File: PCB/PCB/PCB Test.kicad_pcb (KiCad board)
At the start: 2 copper layers, 69 x 30 mm, 53 parts, among them J1 USB_C_Receptacle_USB2.0, J2 Conn_01x06, J3 BATT, Q1 DMN2056U, Q2 Si2329DS, Q3 DMN2056U, Q4 DMG9926UDM, SW1 SW_Push, SW2 SW_Push, U1 24FC64F, U2 STM32L052K6Tx, U3 TUSB320, U4 MIC5366-3.3YC5, U5 BQ297xy, U6 BQ24072RGT

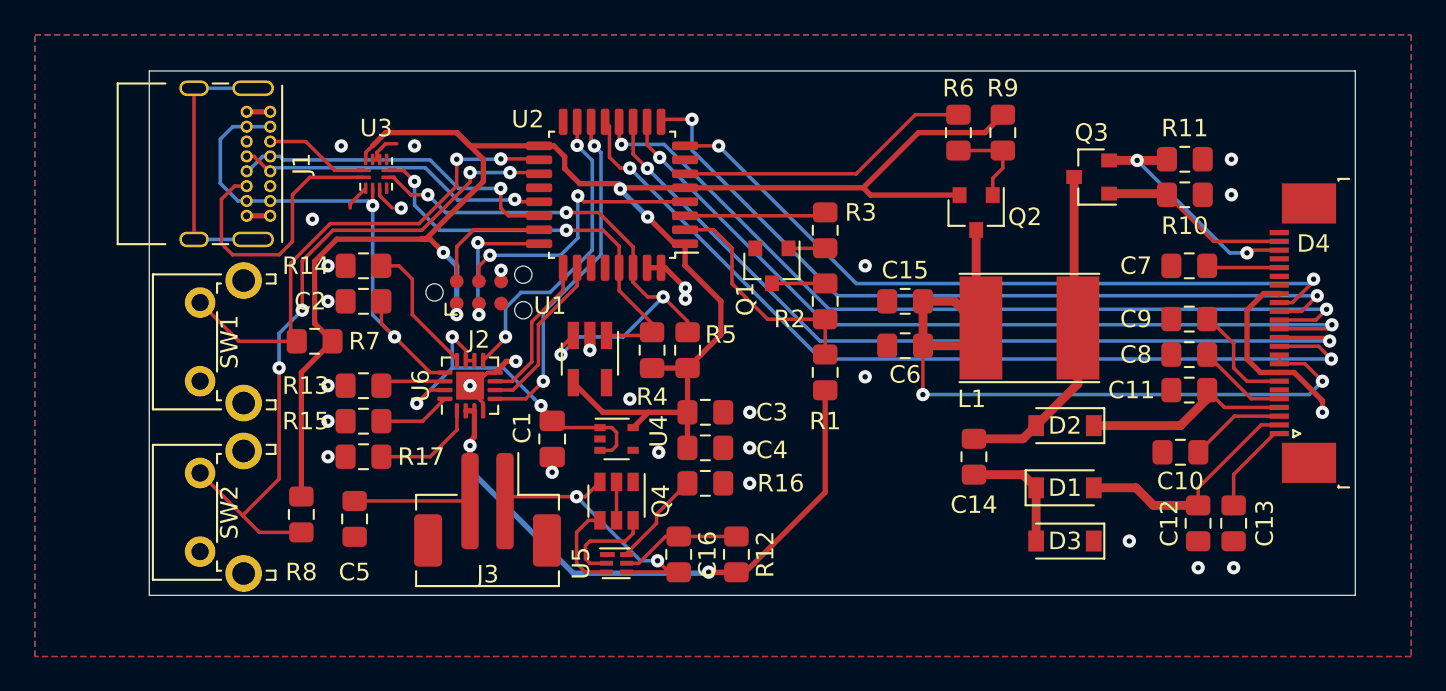
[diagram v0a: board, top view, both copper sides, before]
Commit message: Updated schematic to Rev C
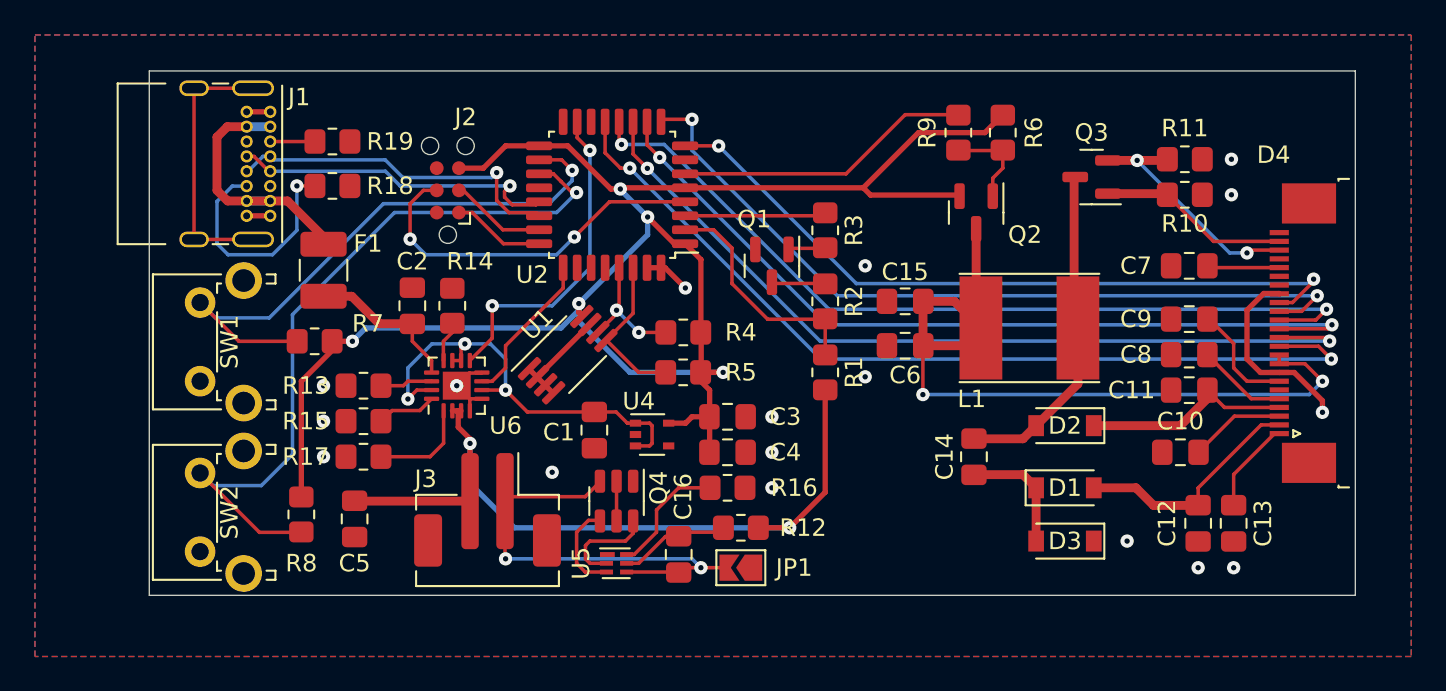
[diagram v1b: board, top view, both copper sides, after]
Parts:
- removed U3: TUSB320, Package_DFN_QFN:Texas_X2QFN-12_1.6x1.6mm_P0.4mm
- added F1: Polyfuse, Fuse:Fuse_1210_3225Metric_Pad1.42x2.65mm_HandSolder, F.Cu at (141.0, 41.4)
- added JP1: Jumper_2_Open, Jumper:SolderJumper-2_P1.3mm_Open_TrianglePad1.0x1.5mm, F.Cu at (164.8, 58.4)
- added R18: 5.1k, Resistor_SMD:R_0805_2012Metric_Pad1.20x1.40mm_HandSolder, F.Cu at (141.5, 36.6)
- added R19: 5.1k, Resistor_SMD:R_0805_2012Metric_Pad1.20x1.40mm_HandSolder, F.Cu at (141.5, 34.0)
- C10, C11, C12, C13, C14, C15, C16, C2, C3, C4, C5, C6, C7, C8, C9: footprint Capacitor_SMD:C_0805_2012Metric_Pad1.15x1.40mm_HandSolder -> Capacitor_SMD:C_0805_2012Metric_Pad1.18x1.45mm_HandSolder
- R1, R10, R11, R12, R13, R14, R15, R16, R17, R2, R3, R4, R5, R6, R7, R8, R9: footprint Resistor_SMD:R_0805_2012Metric_Pad1.15x1.40mm_HandSolder -> Resistor_SMD:R_0805_2012Metric_Pad1.20x1.40mm_HandSolder
- U1: value 24FC64F -> 24LC256; footprint Package_TO_SOT_SMD:SOT-23-5_HandSoldering -> Package_SO:MSOP-8_3x3mm_P0.65mm
- U2: value STM32L052K6Tx -> STM32L072KZTx
- moved J2 6.11 mm to (148.1, 36.8), turned to 90 degrees
- moved R14 5.57 mm to (148.3, 43.4), turned to 90 degrees
- moved C2 2.81 mm to (146.1, 43.4), turned to 90 degrees
- moved C1 2.47 mm to (156.5, 50.5)
- moved R4 2.06 mm to (161.6, 45.0), turned to 180 degrees
- moved U4 2.05 mm to (159.8, 50.8)
- moved R12 1.55 mm to (164.8, 56.1), turned to 0 degrees
- moved C4 1.30 mm to (164.1, 51.8)
- moved C3 1.30 mm to (164.1, 49.8)
- moved R16 1.30 mm to (164.1, 53.8)
- moved U1 1.30 mm to (154.9, 46.2), turned to 45 degrees
- moved R5 1.30 mm to (161.5, 47.2), turned to 180 degrees
- moved U6 0.76 mm to (148.6, 48.0)
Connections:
- D4 pad 1: Net-(D4-Pad1) -> unconnected-(D4-Pad1)
- D4 pad 4: Net-(D4-Pad4) -> unconnected-(D4-Pad4)
- D4 pad 6: Net-(D4-Pad6) -> unconnected-(D4-Pad6)
- D4 pad 7: Net-(D4-Pad7) -> unconnected-(D4-Pad7)
- J1 pad A4: VBUS -> Net-(F1-Pad1)
- J1 pad A5: CC1 -> Net-(J1-PadA5)
- J1 pad A8: Net-(J1-PadA8) -> unconnected-(J1-PadA8)
- J1 pad A9: VBUS -> Net-(F1-Pad1)
- J1 pad B4: VBUS -> Net-(F1-Pad1)
- J1 pad B5: CC2 -> Net-(J1-PadB5)
- J1 pad B8: Net-(J1-PadB8) -> unconnected-(J1-PadB8)
- J1 pad B9: VBUS -> Net-(F1-Pad1)
- J1 pad S1: Net-(J1-PadS1) -> unconnected-(J1-PadS1)
- J2 pad 1: +3V3 -> SWCLK
- J2 pad 2: SWDIO -> unconnected-(J2-Pad2)
- J2 pad 3: SWCLK -> SWDIO
- J2 pad 5: Net-(J2-Pad5) -> +3V3
- Q4 pad 2: Net-(Q4-Pad2) -> unconnected-(Q4-Pad2)
- Q4 pad 5: Net-(Q4-Pad2) -> unconnected-(Q4-Pad2)
- U1 pad 1: SCL -> GND
- U1 pad 3: SDA -> GND
- U1 pad 4: +3V3 -> GND
- U1 pad 5: GND -> SDA
- U2 pad 14: CHR_EN2 -> unconnected-(U2-Pad14)
- U2 pad 20: Net-(U2-Pad20) -> unconnected-(U2-Pad20)
- U2 pad 26: CHR_EN1 -> unconnected-(U2-Pad26)
- U2 pad 27: Net-(U2-Pad27) -> unconnected-(U2-Pad27)
- U2 pad 28: Net-(U2-Pad28) -> unconnected-(U2-Pad28)
- U2 pad 7: Net-(U2-Pad7) -> unconnected-(U2-Pad7)
- U4 pad 4: Net-(U4-Pad4) -> unconnected-(U4-Pad4)
- U5 pad 1: Net-(U5-Pad1) -> unconnected-(U5-Pad1)
- U6 pad 5: CHR_EN2 -> GND
- U6 pad 6: CHR_EN1 -> VCC
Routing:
- net SDA: track 30.9 -> 8.91 mm, vias 4 -> 0
- net VBUS: track 30.0 -> 8.98 mm, vias 2 -> 0
- net CHR_EN2: track 19.6 -> 0.00 mm, vias 2 -> 0
- net SCL: track 24.2 -> 7.66 mm
- net CC2: track 16.1 -> 0.00 mm
- net unconnected-(J1-PadS1): track 0.00 -> 15.4 mm
- net Net-(J1-PadS1): track 15.4 -> 0.00 mm
- net Net-(F1-Pad1): track 0.00 -> 15.3 mm
- net Net-(J1-PadB5): track 0.00 -> 13.5 mm, vias 0 -> 1
- net Net-(C16-Pad2): track 16.5 -> 26.5 mm
- net CHR_EN1: track 9.54 -> 0.00 mm
- net +3V3: track 111.1 -> 104.3 mm, vias 4 -> 5
- net CC1: track 6.02 -> 0.00 mm
- net Net-(R14-Pad1): track 7.80 -> 2.32 mm
- net BT1: track 28.7 -> 34.1 mm, vias 2 -> 1
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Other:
- rule pad_to_mask_clearance: 0.0508 -> 0
- board text added: "ePaper Name Tag Rev C"
- board text removed: "ePaper Name Tag Rev B"
